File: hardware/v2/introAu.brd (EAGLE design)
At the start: 50 x 50 mm, 23 parts

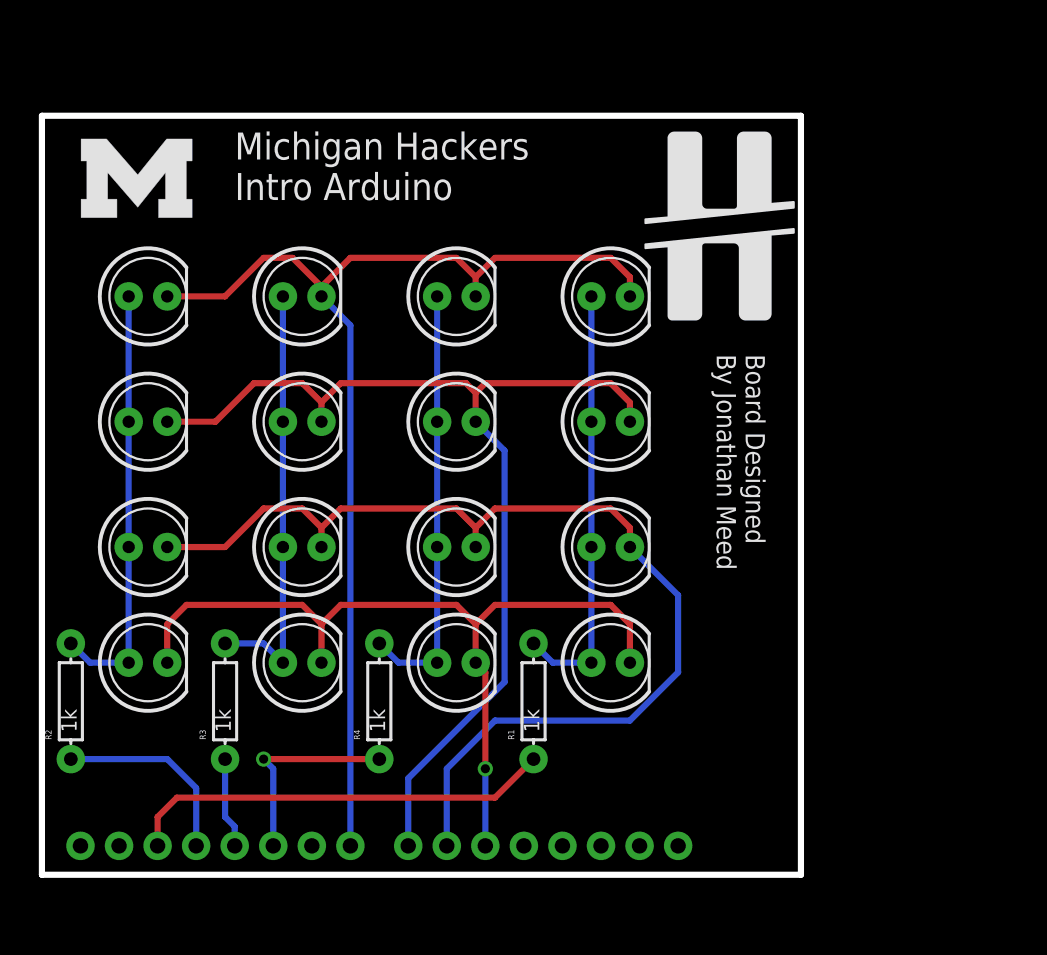
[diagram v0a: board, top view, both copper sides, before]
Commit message: Added potentiometer, button, surface mount LEDs to v2
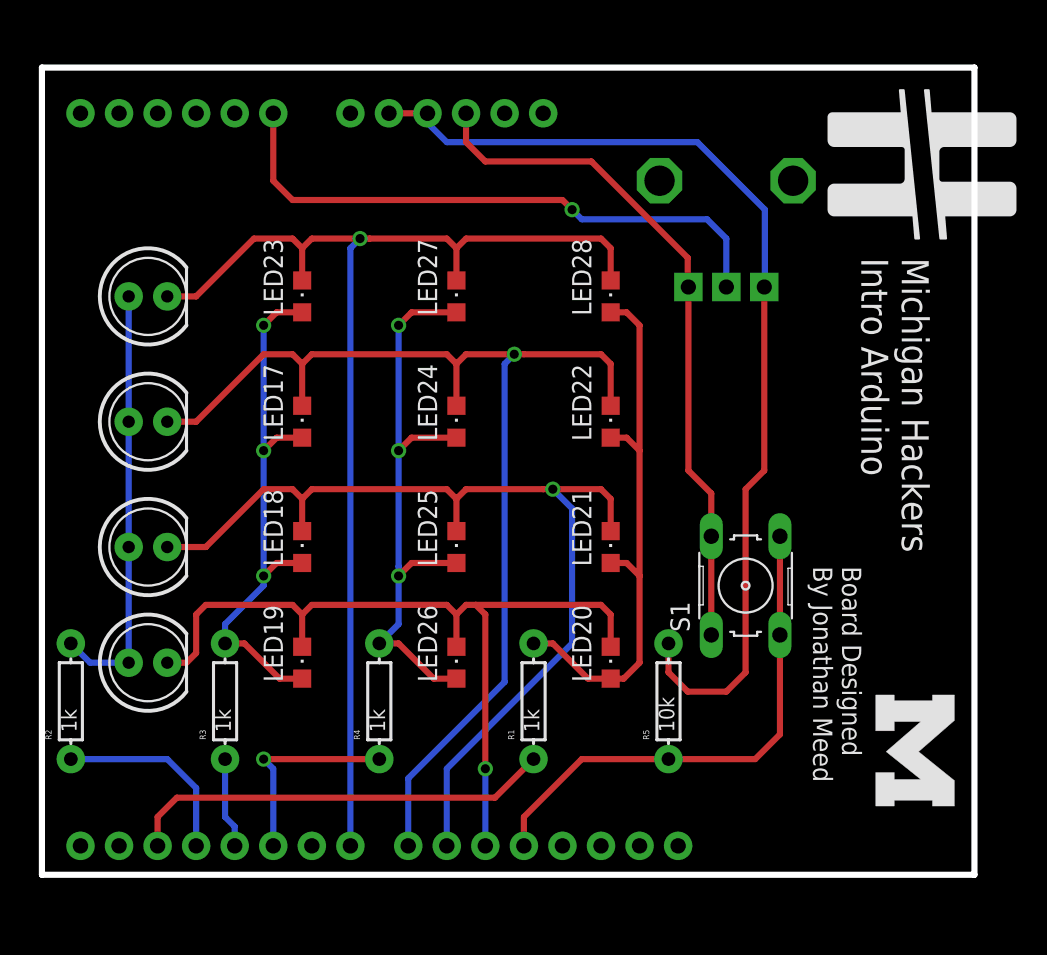
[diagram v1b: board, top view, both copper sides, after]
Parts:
- removed LED1, LED11, LED12, LED13, LED15, LED16, LED2, LED3, LED5, LED6, LED7, LED8: (no value), SparkFun-LED:LED5MM
- added LED17, LED18, LED19, LED20, LED21, LED22, LED23, LED24, LED25, LED26, LED27, LED28: (no value), led:CHIPLED_0805
- added R5: 10k, SparkFun-Resistors:AXIAL-0.3EZ
- added S1: (no value), MESH_Arduino:B3F-10XX
- added U$5: (no value), SparkFun-Electromechanical:ALPS_POT
- moved U$2 60.4 mm to (54.6, 11.2), turned to 270 degrees
- moved U$3 17.2 mm to (52.1, 50.2), turned to 270 degrees
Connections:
- new net +5V: S1.1, S1.2, U$1.5V, U$5.P$1
- new net BUTTON: R5.P$1, S1.3, S1.4, U$1.D11
- new net GND: R5.P$2, U$1.GND@0, U$1.GND@1, U$5.P$3
- new net POT: U$1.A0, U$5.P$2
- net COL1: now also LED23.C, LED27.C, LED28.C; no longer LED1.K, LED12.K, LED6.K
- net COL2: now also LED17.C, LED22.C, LED24.C; no longer LED13.K, LED2.K, LED7.K
- net COL3: now also LED18.C, LED21.C, LED25.C; no longer LED15.K, LED3.K, LED8.K
- net COL4: now also LED19.C, LED20.C, LED26.C; no longer LED11.K, LED16.K, LED5.K
- net ROW1: now also LED20.A, LED21.A, LED22.A, LED28.A; no longer LED12.A, LED13.A, LED15.A, LED16.A
- net ROW3: now also LED17.A, LED18.A, LED19.A, LED23.A; no longer LED1.A, LED2.A, LED3.A, LED5.A
- net ROW4: now also LED24.A, LED25.A, LED26.A, LED27.A; no longer LED11.A, LED6.A, LED7.A, LED8.A
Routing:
- net GND: track 0.00 -> 66.8 mm
- net +5V: track 0.00 -> 45.1 mm
- net POT: track 0.00 -> 39.1 mm, vias 0 -> 1
- net BUTTON: track 0.00 -> 34.1 mm
- net ROW4: track 28.5 -> 40.0 mm, vias 0 -> 3
- net ROW1: track 29.1 -> 37.4 mm
- net ROW3: track 28.5 -> 36.7 mm, vias 0 -> 3
- net COL2: track 69.4 -> 75.9 mm, vias 0 -> 1
- net COL3: track 70.5 -> 65.9 mm, vias 0 -> 1
- net COL1: track 74.8 -> 78.7 mm, vias 0 -> 1
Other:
- board size 50 x 50 mm -> 61.4 x 53.2 mm

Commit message: Merged in Leonardo onboard
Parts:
- removed R3, R4: 1k, SparkFun-Resistors:AXIAL-0.3EZ
- removed U$1: ARDUINO_SHIELDNO_SILK, SparkFun-Boards:DUEMILANOVE_VIAS
- added C1, C2: 100nF, rcl:C0805
- added JP1, JP2: (no value), SparkFun-Connectors:1X06_SMD_STRAIGHT_COMBO
- added JP3, JP4: (no value), SparkFun-Connectors:1X08_SMD_COMBINED
- added JP5: (no value), SparkFun-Connectors:2X3
- added L1: (no value), EagleLibrary_Wuerth_Elektronik_eiSos_rev15c:WE-CBF_0805(W=3.0)
- added LED1: (no value), led:CHIPLED_0805
- added Q1: CERAMIC_RESONATOR_SMD6M00G53Z, MESH_Arduino:CERAMIC_RESONATOR_SMD
- added R10, R8, R9: 1k, rcl:R0805
- added R6, R7: 22, rcl:R0805
- added Z1: zenor 3.6w, rcl:R0603
- added Z2: zener 3.6w, rcl:R0603
- R1: device SparkFun-Resistors:AXIAL-0.3EZ -> rcl:R0805
- U$2: value (none) -> ATMEGA32U4TQFP; device artwork:SMALL-M -> SparkFun-DigitalIC:SPARKFUN-DIGITALIC_TQFP44
- U$3: value (none) -> USB_MICROB_0001LF; device artwork:SMALL-MH -> mBLE:USB_MICROB_CHEAPER
- moved U$3 58.9 mm to (5.84, 13.7)
- moved R2 50.4 mm to (51.7, 3.81), turned to 0 degrees
- moved LED10 49.8 mm to (56.8, 21.8)
- moved LED14 49.8 mm to (56.8, 14.2)
- moved LED4 49.8 mm to (56.8, 38.4)
- moved LED9 49.8 mm to (56.8, 30.1)
- moved S1 45.1 mm to (6.73, 40.5)
- moved U$2 40.1 mm to (17.4, 26.0), turned to 0 degrees
- moved R5 38.6 mm to (17.1, 41.6)
- moved R1 33.0 mm to (4.24, 28.7), turned to 0 degrees
- moved LED17 24.4 mm to (41.5, 30.1)
- moved LED18 24.4 mm to (41.5, 21.8)
- moved LED19 24.4 mm to (41.5, 14.2)
- moved LED23 24.4 mm to (41.5, 38.4)
- moved LED24 21.8 mm to (49.1, 30.1)
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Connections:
- removed net N$16: R1.P$1, U$1.D2
- removed net N$17: R2.P$1, U$1.D3
- removed net N$18: R3.P$1, U$1.D4
- removed net N$19: R4.P$1, U$1.D5
- new net +3V3: JP2.2
- new net A0: JP1.1
- new net A1: JP1.2, U$2.37
- new net A2: JP1.3, U$2.38
- new net A3: JP1.4, U$2.39
- new net A4: JP1.5, U$2.40
- new net A5: JP1.6, U$2.41
- new net AREF: C2.1, JP4.1, L1.2, U$2.42
- new net D0: JP3.8, U$2.20
- new net D1: JP3.7, U$2.21
- new net D10: JP4.6
- new net D11: JP4.5, U$2.12
- new net D12: JP4.4, U$2.26
- new net D13: JP4.3, U$2.32
- new net D14: U$2.11
- new net D15: U$2.9
- new net D16: U$2.10
- new net D17: U$2.8
- new net D2: JP3.6
- new net D3: JP3.5
- new net D4: JP3.4
- new net D5: JP3.3
- new net D6: JP3.2
- new net D7: JP3.1
- new net D8: JP4.8
- new net D9: JP4.7
- new net MISO: JP5.1
- new net MOSI: JP5.4
- new net N$1: R10.1, U$2.19
- new net N$11: LED1.A, R1.1
- new net N$2: R2.P$1, U$2.18
- new net N$3: R9.1, U$2.25
- new net N$4: R8.1, U$2.31
- new net N$5: Q1.3, U$2.16
- new net N$6: Q1.1, U$2.17
- new net N$7: R7.1, U$3.P$2, Z2.2
- new net N$9: R6.1, U$3.P$3, Z1.2
- new net RD+: R6.2, U$2.4
- new net RD-: R7.2, U$2.3
- new net RESET: JP2.1, JP5.5, U$2.13
- new net SCK: JP5.3
- new net TX: U$2.22
- new net VIN: JP2.6
- net +5V: now also C1.1, JP2.3, JP5.2, L1.1, R1.2, U$2.14, U$2.2, U$2.24, U$2.34, U$2.44, U$2.7, U$3.P$1; no longer U$1.5V
- net BUTTON: now also U$2.30; no longer U$1.D11
- net COL1: now also U$2.27; no longer U$1.D7
- net COL2: now also U$2.1; no longer U$1.D8
- net COL3: now also U$2.28; no longer U$1.D9
- net COL4: now also U$2.29; no longer U$1.D10
- net GND: now also C1.2, C2.2, JP2.4, JP2.5, JP4.2, JP5.6, LED1.C, Q1.2, U$2.15, U$2.23, U$2.35, U$2.43, U$2.5, U$2.6, U$3.P$4, Z1.1, Z2.1; no longer U$1.GND@0, U$1.GND@1
- net POT: now also U$2.36; no longer U$1.A0
- net ROW1: now also R10.2; no longer R1.P$2
- net ROW3: now also R9.2; no longer R3.P$2
- net ROW4: now also R8.2; no longer R4.P$2
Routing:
- net AREF: track 0.00 -> 72.5 mm, vias 0 -> 2
- net GND: track 66.8 -> 9.69 mm, vias 0 -> 2
- net RESET: track 0.00 -> 54.2 mm, vias 0 -> 2
- net D13: track 0.00 -> 50.3 mm, vias 0 -> 4
- net N$3: track 0.00 -> 45.8 mm, vias 0 -> 4
- net N$4: track 0.00 -> 42.9 mm, vias 0 -> 2
- net D11: track 0.00 -> 41.4 mm, vias 0 -> 2
- net N$2: track 0.00 -> 39.0 mm
- net D1: track 0.00 -> 35.1 mm, vias 0 -> 2
- net D0: track 0.00 -> 32.4 mm, vias 0 -> 2
- net D12: track 0.00 -> 30.2 mm, vias 0 -> 2
- net COL1: track 78.7 -> 50.4 mm, vias 1 -> 0
- net N$16: track 28.2 -> 0.00 mm
- net N$7: track 0.00 -> 26.3 mm, vias 0 -> 2
- net A4: track 0.00 -> 26.2 mm
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- added copper zone on layer 16, net +5V
- added copper zone on layer 1, net GND
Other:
- board size 61.4 x 53.2 mm -> 61.5 x 56.4 mm
- board text removed: "Board Designed By Jonathan Meed"
- board text removed: "Michigan Hackers Intro Arduino"
